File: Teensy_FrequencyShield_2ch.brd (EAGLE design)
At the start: 17 parts, among them IC9 78L05F

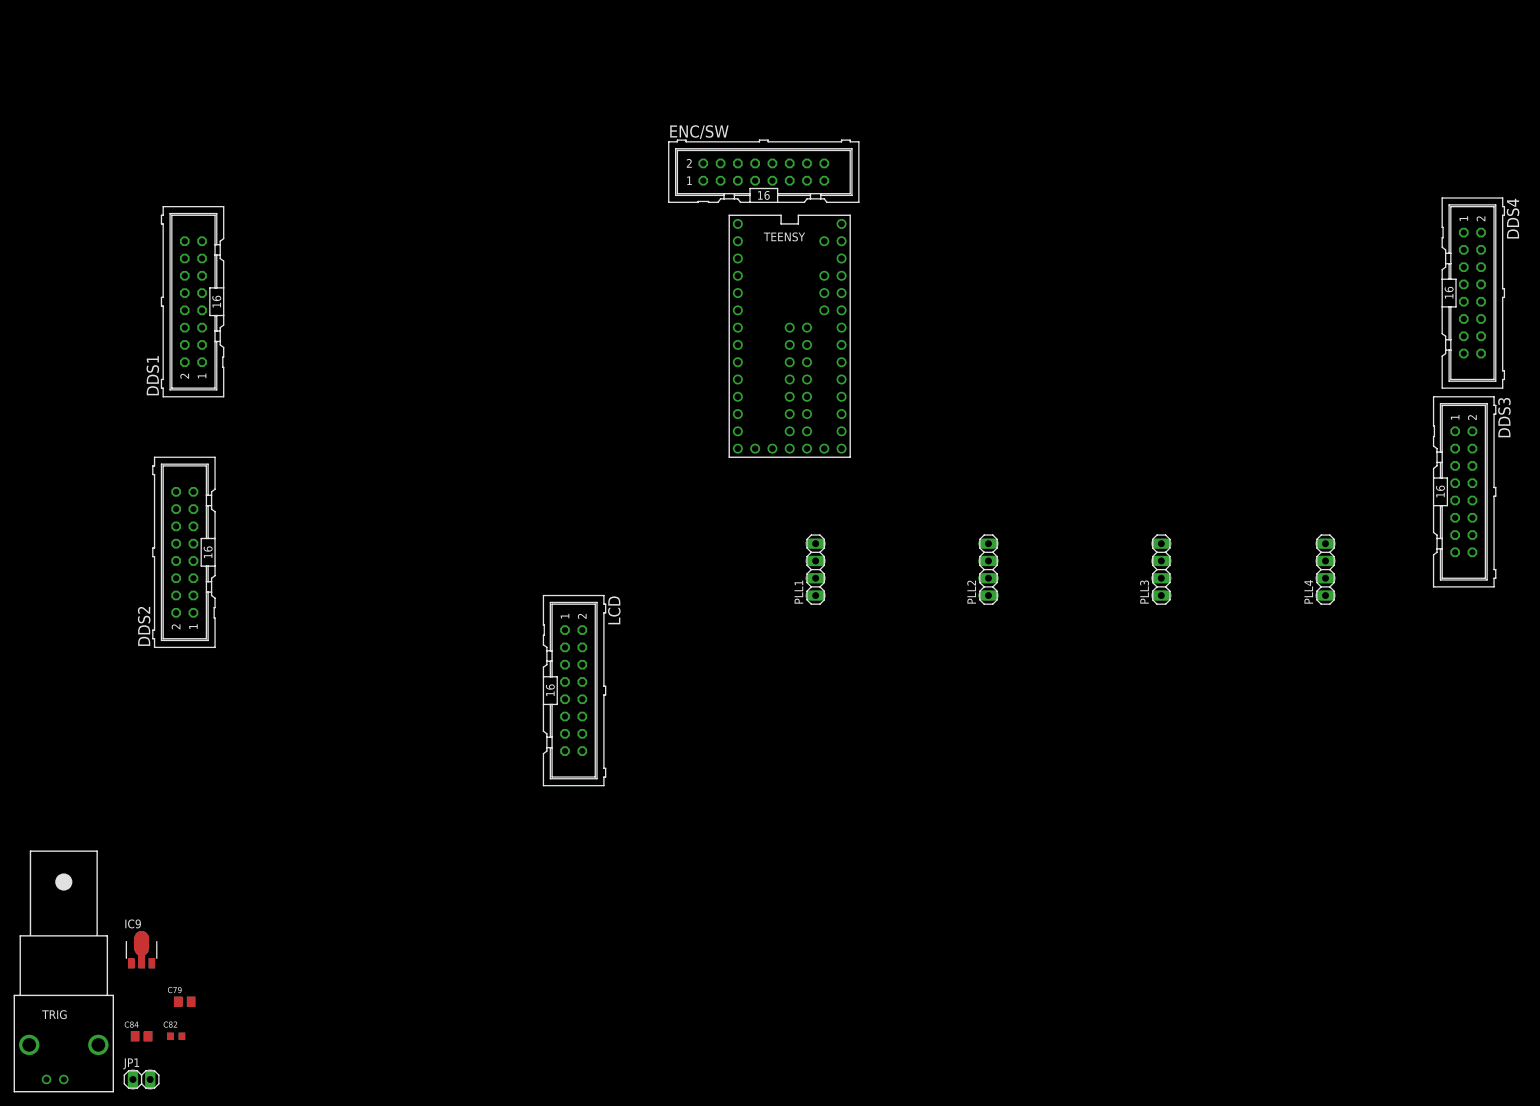
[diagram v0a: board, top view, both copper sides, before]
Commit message: teensy board with two dds channels and 2 plls
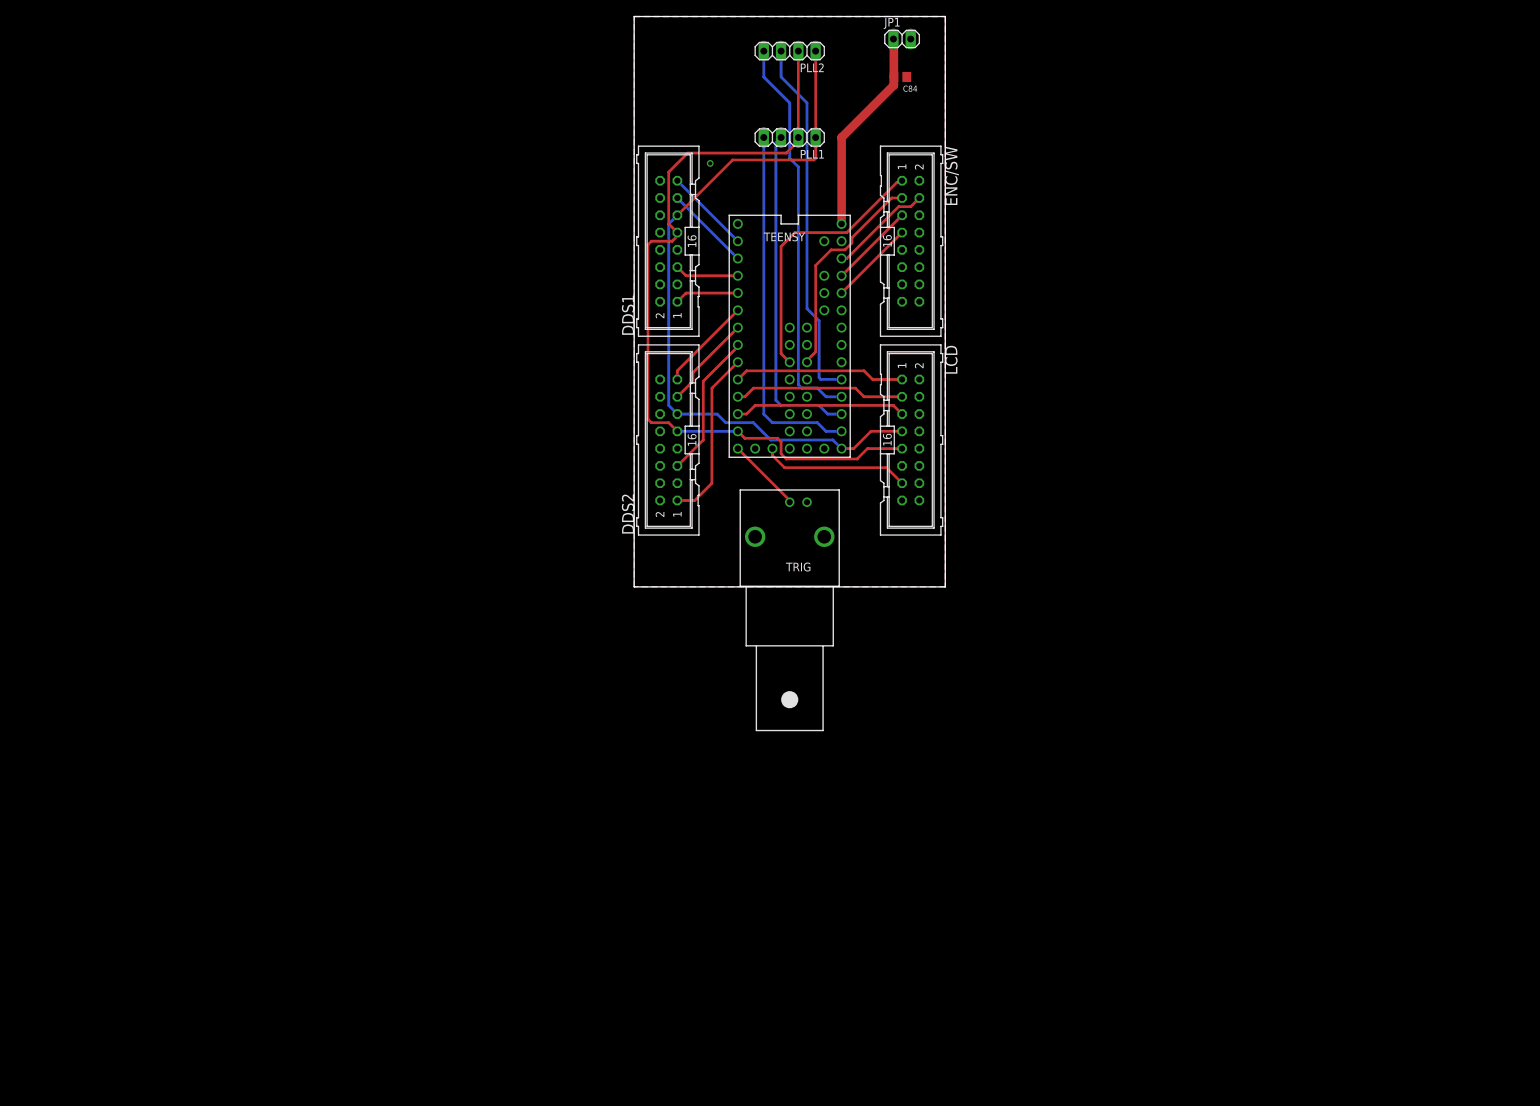
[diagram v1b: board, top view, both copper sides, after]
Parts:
- removed C79: 1uF, rlc-jqi:0805
- removed C82: 100nF, rlc-jqi:0603
- removed DDS3, DDS4: (no value), mcu-accessories:ML16
- removed IC9: 78L05F, aom_driver:SOT89
- removed PLL3, PLL4: (no value), pinhead:1X04
- moved JP1 189.4 mm to (-6.35, 50.0)
- moved C84 179.7 mm to (-6.60, 44.5), turned to 180 degrees
- moved TRIG 130.2 mm to (-22.9, -23.1), turned to 180 degrees
- moved PLL2 81.6 mm to (-22.9, 48.3), turned to 180 degrees
- moved DDS2 73.0 mm to (-40.6, -8.89)
- moved DDS1 70.4 mm to (-40.6, 20.3)
- moved PLL1 63.6 mm to (-22.9, 35.6), turned to 180 degrees
- moved LCD 61.7 mm to (-5.08, -8.89)
- moved ENC/SW 23.9 mm to (-5.08, 20.3), turned to 270 degrees
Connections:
- removed net DDS3_CS: DDS3.13, TEENSY.15/A1
- removed net DDS3_IOUPDATE: DDS3.1, TEENSY.17/A3
- removed net DDS3_PS0: DDS3.5, TEENSY.16/A2
- removed net DDS3_RESET: DDS3.15, TEENSY.14/A0
- removed net PLL3_LE: PLL3.3, TEENSY.32
- removed net PLL3_MUX: PLL3.4, TEENSY.28
- removed net PLL4_LE: PLL4.3, TEENSY.33
- removed net PLL4_MUX: PLL4.4, TEENSY.29
- removed net V+: C79.1, C84.2, IC9.3, JP1.1
- net +5V: now also C84.2, JP1.1; no longer C82.2, IC9.1
- net CLK: no longer DDS3.11, DDS4.11, PLL3.1, PLL4.1
- net DDS4_CS: no longer DDS4.13
- net DDS4_IOUPDATE: no longer DDS4.1
- net DDS4_PS0: no longer DDS4.5
- net DDS4_RESET: no longer DDS4.15
- net GND: no longer C79.2, C82.1, DDS3.10, DDS3.12, DDS3.14, DDS3.16, DDS3.2, DDS3.3, DDS3.4, DDS3.6, DDS3.7, DDS3.8, DDS4.10, DDS4.12, DDS4.14, DDS4.16, DDS4.2, DDS4.3, DDS4.4, DDS4.6, DDS4.7, DDS4.8, IC9.2, IC9.2@1
- net MOSI: no longer DDS3.9, DDS4.9, PLL3.2, PLL4.2
- net PLL1_LE: now also TEENSY.15/A1; no longer TEENSY.30
- net PLL1_MUX: now also TEENSY.14/A0; no longer TEENSY.26
- net PLL2_LE: now also TEENSY.17/A3; no longer TEENSY.31
- net PLL2_MUX: now also TEENSY.16/A2; no longer TEENSY.27
- net SW1: now also TEENSY.33; no longer TEENSY.25
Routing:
- net MOSI: track 0.00 -> 116.0 mm
- net CLK: track 0.00 -> 106.0 mm
- net PLL2_MUX: track 0.00 -> 58.2 mm
- net PLL2_LE: track 0.00 -> 53.7 mm
- net PLL1_MUX: track 0.00 -> 53.1 mm
- net PLL1_LE: track 0.00 -> 49.4 mm
- net ENC_SW: track 0.00 -> 39.3 mm
- net VDD: track 0.00 -> 36.9 mm
- net SW1: track 0.00 -> 32.0 mm
- net +5V: track 0.00 -> 30.4 mm
- net DDS2_IOUPDATE: track 0.00 -> 25.5 mm
- net LCD_RS: track 0.00 -> 25.2 mm
- net LCD_RST: track 0.00 -> 25.2 mm
- net LCD_CSB: track 0.00 -> 25.2 mm
- net DDS2_PS0: track 0.00 -> 21.5 mm
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- added copper zone on layer 1, net GND
- added copper zone on layer 16, net GND
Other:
- board outline added: 45.7 x 83.8 mm

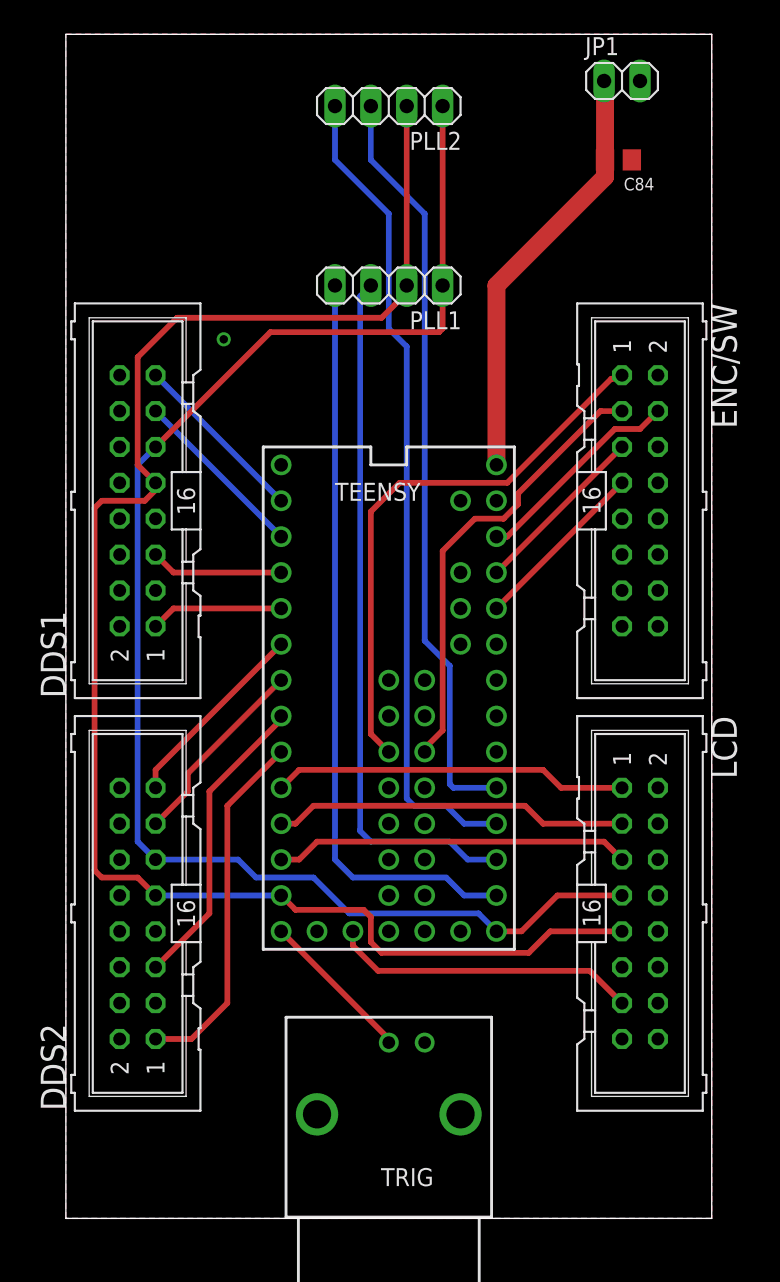
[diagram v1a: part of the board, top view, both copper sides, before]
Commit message: Tweaked pin layout; added back in extra DDS & PLL channel names to Teensy pinout
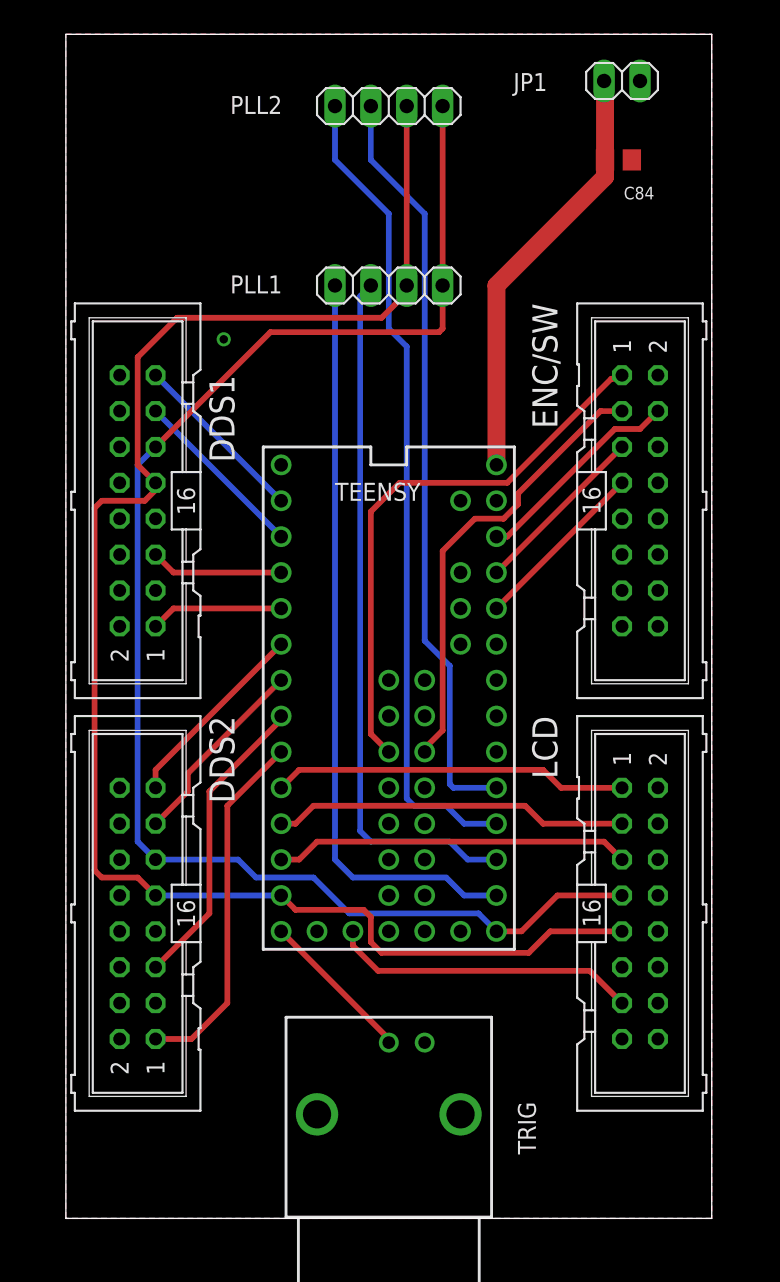
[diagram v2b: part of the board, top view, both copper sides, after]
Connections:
- new net DDS3_CS: TEENSY.26
- new net DDS3_IOUPDATE: TEENSY.28
- new net DDS3_PS0: TEENSY.27
- new net DDS3_RESET: TEENSY.25
- new net PLL3_LE: TEENSY.30
- new net PLL3_MUX: TEENSY.29
- new net PLL4_LE: TEENSY.32
- new net PLL4_MUX: TEENSY.31
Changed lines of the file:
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@@
 <?xml version="1.0" encoding="utf-8"?>
 <!DOCTYPE eagle SYSTEM "eagle.dtd">
-<eagle version="6.2">
+<eagle version="6.5.0">
 <drawing>
 <settings>
@@
 </class>
 </classes>
-<designrules>
+<designrules name="default">
 <description language="de">&lt;b&gt;EAGLE Design Rules&lt;/b&gt;
 &lt;p&gt;
@@
 </autorouter>
 <elements>
-<element name="TEENSY" library="mcu-accessories" package="TEENSY_3.1_ALLPINS" value="TEENSY_3.1_ALL_PINS_AND_PADS" x="-22.86" y="5.08"/>
-<element name="LCD" library="mcu-accessories" package="ML16" value="" x="-5.08" y="-8.89" rot="R270">
+<element name="TEENSY" library="mcu-accessories" package="TEENSY_3.1_ALLPINS" value="TEENSY_3.1_ALL_PINS_AND_PADS" x="-22.86" y="5.08" smashed="yes">
+<attribute name="NAME" x="-26.67" y="20.32" size="1.27" layer="25" font="vector"/>
+</element>
+<element name="LCD" library="mcu-accessories" package="ML16" value="" x="-5.08" y="-8.89" smashed="yes" rot="R270">
 <attribute name="OC_NEWARK" value="unknown" x="-5.08" y="-8.89" size="1.778" layer="27" rot="R270" display="off"/>
 <attribute name="PARTNO" value="S9171-ND" x="-5.08" y="-8.89" size="1.778" layer="27" rot="R270" display="off"/>
@@
 <attribute name="MF" value="" x="-5.08" y="-8.89" size="1.778" layer="27" rot="R270" display="off"/>
 <attribute name="OC_FARNELL" value="unknown" x="-5.08" y="-8.89" size="1.778" layer="27" rot="R270" display="off"/>
-</element>
-<element name="PLL1" library="pinhead" package="1X04" value="" x="-22.86" y="35.56" rot="R180"/>
-<element name="PLL2" library="pinhead" package="1X04" value="" x="-22.86" y="48.26" rot="R180"/>
-<element name="DDS1" library="mcu-accessories" package="ML16" value="" x="-40.64" y="20.32" rot="R90">
+<attribute name="NAME" x="-12.7" y="5.08" size="1.778" layer="25" ratio="10" rot="R270"/>
+<attribute name="VALUE" x="0" y="-10.16" size="1.778" layer="27" ratio="10" rot="R270"/>
+</element>
+<element name="PLL1" library="pinhead" package="1X04" value="" x="-22.86" y="35.56" smashed="yes" rot="R180">
+<attribute name="NAME" x="-30.4038" y="36.2712" size="1.27" layer="25" ratio="10" rot="R180"/>
+<attribute name="VALUE" x="-17.78" y="38.735" size="1.27" layer="27" rot="R180"/>
+</element>
+<element name="PLL2" library="pinhead" package="1X04" value="" x="-22.86" y="48.26" smashed="yes" rot="R180">
+<attribute name="NAME" x="-30.4038" y="48.9712" size="1.27" layer="25" ratio="10" rot="R180"/>
+<attribute name="VALUE" x="-17.78" y="51.435" size="1.27" layer="27" rot="R180"/>
+</element>
+<element name="DDS1" library="mcu-accessories" package="ML16" value="" x="-40.64" y="20.32" smashed="yes" rot="R90">
 <attribute name="OC_NEWARK" value="unknown" x="-40.64" y="20.32" size="1.778" layer="27" rot="R90" display="off"/>
 <attribute name="MPN" value="" x="-40.64" y="20.32" size="1.778" layer="27" rot="R90" display="off"/>
 <attribute name="MF" value="" x="-40.64" y="20.32" size="1.778" layer="27" rot="R90" display="off"/>
 <attribute name="OC_FARNELL" value="unknown" x="-40.64" y="20.32" size="1.778" layer="27" rot="R90" display="off"/>
-</element>
-<element name="DDS2" library="mcu-accessories" package="ML16" value="" x="-40.64" y="-8.89" rot="R90">
+<attribute name="NAME" x="-35.56" y="29.21" size="1.778" layer="25" ratio="10" rot="R270"/>
+<attribute name="VALUE" x="-45.72" y="21.59" size="1.778" layer="27" ratio="10" rot="R90"/>
+</element>
+<element name="DDS2" library="mcu-accessories" package="ML16" value="" x="-40.64" y="-8.89" smashed="yes" rot="R90">
 <attribute name="OC_NEWARK" value="unknown" x="-40.64" y="-8.89" size="1.778" layer="27" rot="R90" display="off"/>
 <attribute name="MPN" value="" x="-40.64" y="-8.89" size="1.778" layer="27" rot="R90" display="off"/>
 <attribute name="MF" value="" x="-40.64" y="-8.89" size="1.778" layer="27" rot="R90" display="off"/>
 <attribute name="OC_FARNELL" value="unknown" x="-40.64" y="-8.89" size="1.778" layer="27" rot="R90" display="off"/>
-</element>
-<element name="ENC/SW" library="mcu-accessories" package="ML16" value="" x="-5.08" y="20.32" rot="R270">
+<attribute name="NAME" x="-35.56" y="5.08" size="1.778" layer="25" ratio="10" rot="R270"/>
+<attribute name="VALUE" x="-45.72" y="-7.62" size="1.778" layer="27" ratio="10" rot="R90"/>
+</element>
+<element name="ENC/SW" library="mcu-accessories" package="ML16" value="" x="-5.08" y="20.32" smashed="yes" rot="R270">
 <attribute name="OC_NEWARK" value="unknown" x="-5.08" y="20.32" size="1.778" layer="27" rot="R270" display="off"/>
 <attribute name="MPN" value="" x="-5.08" y="20.32" size="1.778" layer="27" rot="R270" display="off"/>
 <attribute name="MF" value="" x="-5.08" y="20.32" size="1.778" layer="27" rot="R270" display="off"/>
 <attribute name="OC_FARNELL" value="unknown" x="-5.08" y="20.32" size="1.778" layer="27" rot="R270" display="off"/>
-</element>
-<element name="C84" library="rlc-jqi" package="0805" value="10uF" x="-6.604" y="44.45" rot="R180">
+<attribute name="NAME" x="-12.7" y="34.29" size="1.778" layer="25" ratio="10" rot="R270"/>
+<attribute name="VALUE" x="0" y="19.05" size="1.778" layer="27" ratio="10" rot="R270"/>
+</element>
+<element name="C84" library="rlc-jqi" package="0805" value="10uF" x="-6.604" y="44.45" smashed="yes" rot="R180">
 <attribute name="PARTNO" value="1276-2890-1-ND" x="2.286" y="39.37" size="1.778" layer="27" rot="R180" display="off"/>
-</element>
-<element name="JP1" library="pinhead" package="1X02" value="" x="-6.35" y="50.038"/>
-<element name="TRIG" library="connector-jqi" package="BNC90" value="BNC-H" x="-22.86" y="-23.114" rot="R180">
+<attribute name="NAME" x="-4.064" y="42.545" size="0.889" layer="25" rot="R180"/>
+</element>
+<element name="JP1" library="pinhead" package="1X02" value="" x="-6.35" y="50.038" smashed="yes">
+<attribute name="NAME" x="-14.0462" y="49.3268" size="1.27" layer="25" ratio="10"/>
+<attribute name="VALUE" x="-8.89" y="46.863" size="1.27" layer="27"/>
+</element>
+<element name="TRIG" library="connector-jqi" package="BNC90" value="BNC-H" x="-22.86" y="-23.114" smashed="yes" rot="R180">
 <attribute name="DIGIKEY" value="12345" x="-22.86" y="-23.114" size="1.778" layer="27" rot="R180" display="off"/>
+<attribute name="NAME" x="-13.716" y="-22.225" size="1.27" layer="25" rot="R270"/>
 </element>
 </elements>
@@
 <wire x1="-7.554" y1="49.972" x2="-7.62" y2="50.038" width="1.27" layer="1"/>
 </signal>
+<signal name="DDS3_RESET">
+<contactref element="TEENSY" pad="25"/>
+</signal>
+<signal name="DDS3_CS">
+<contactref element="TEENSY" pad="26"/>
+</signal>
+<signal name="DDS3_PS0">
+<contactref element="TEENSY" pad="27"/>
+</signal>
+<signal name="DDS3_IOUPDATE">
+<contactref element="TEENSY" pad="28"/>
+</signal>
+<signal name="PLL3_LE">
+<contactref element="TEENSY" pad="30"/>
+</signal>
+<signal name="PLL4_MUX">
+<contactref element="TEENSY" pad="31"/>
+</signal>
+<signal name="PLL4_LE">
+<contactref element="TEENSY" pad="32"/>
+</signal>
+<signal name="PLL3_MUX">
+<contactref element="TEENSY" pad="29"/>
+</signal>
 </signals>
